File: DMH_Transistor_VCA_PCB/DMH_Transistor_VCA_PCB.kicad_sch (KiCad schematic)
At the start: 0 parts

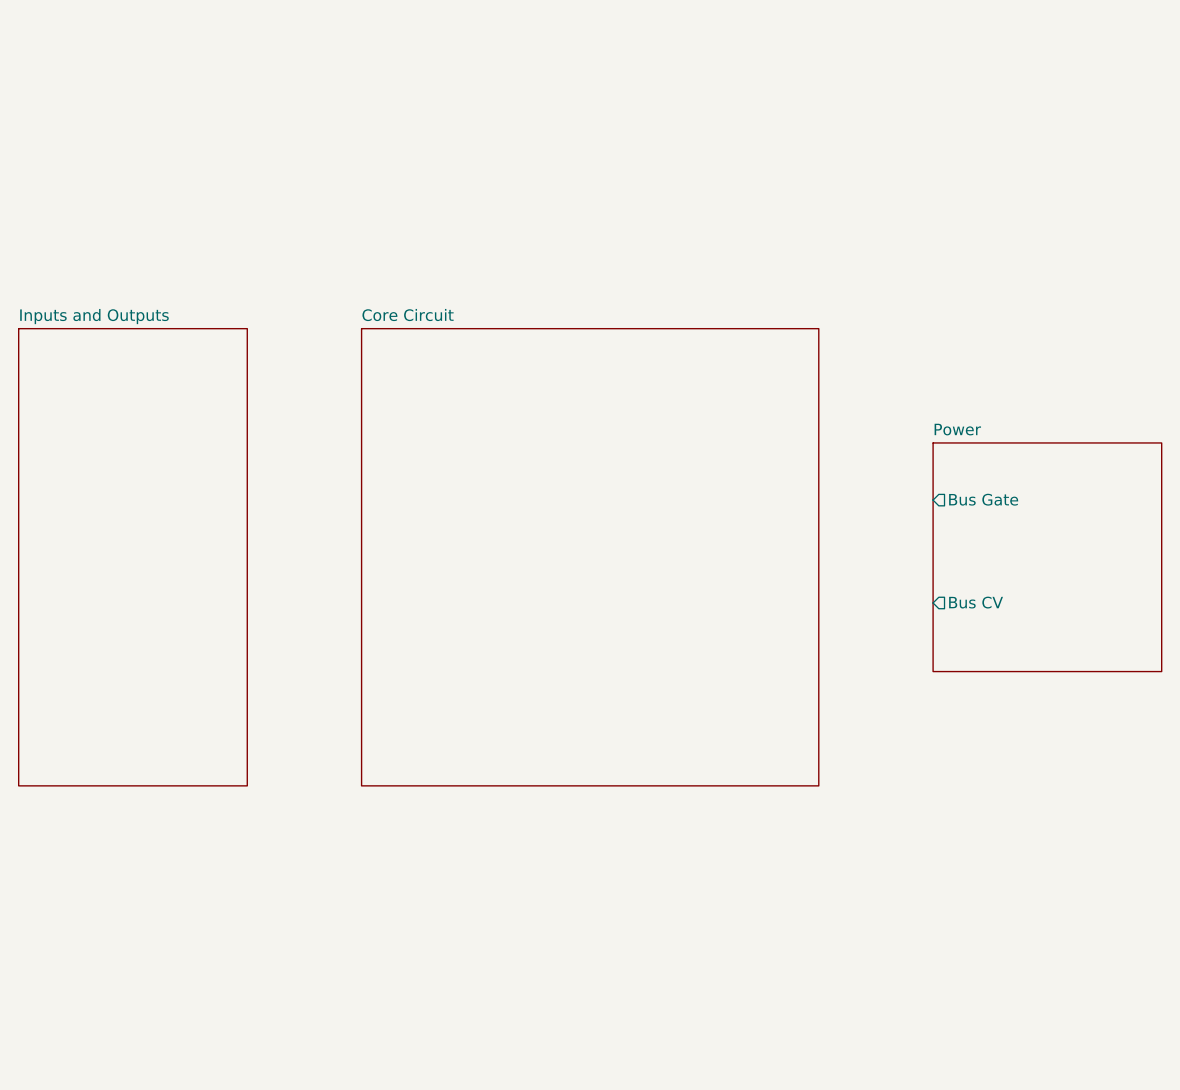
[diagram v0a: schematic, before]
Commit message: Finished core circuit schematic
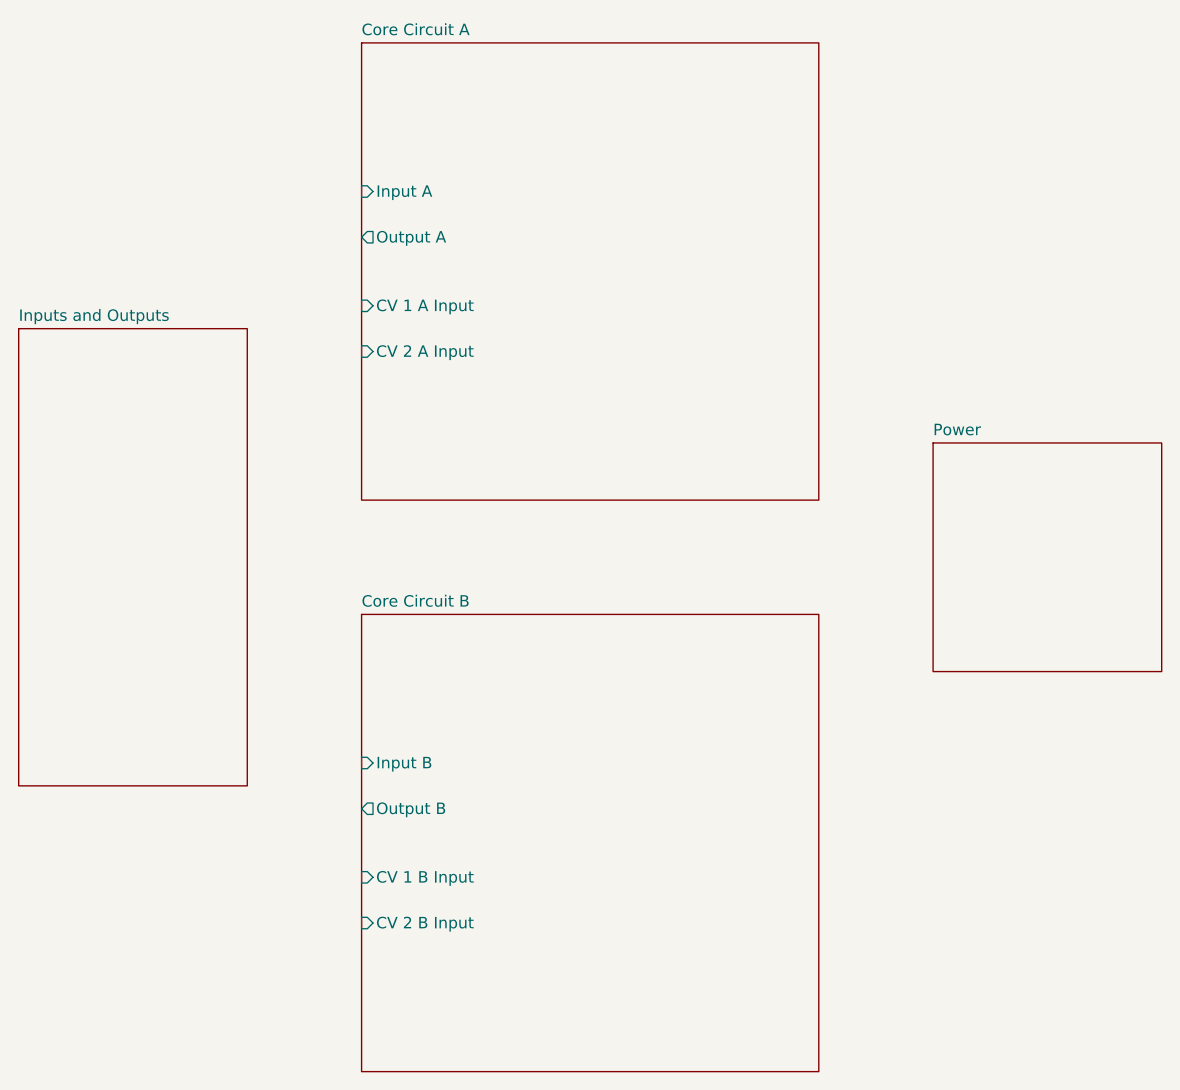
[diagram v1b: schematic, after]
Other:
- sheet Core Circuit renamed Core Circuit A
- added sheet Core Circuit B (Core_Circuit_B.kicad_sch)
- sheet Core Circuit A: file Core_Circuit.kicad_sch -> Core_Circuit_A.kicad_sch
- sheet Core Circuit A ports: added CV 1 A Input, CV 2 A Input, Input A, Output A; removed none
- sheet Power ports: added none; removed Bus CV, Bus Gate
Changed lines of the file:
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@@
-			)
-		)
-		(pin "Bus Gate" output
-			(at 127 95.25 180)
-			(effects
-				(font
-					(size 1.27 1.27)
-				)
-				(justify left)
-			)
-		)
-		(pin "Bus CV" output
-			(at 127 106.68 180)
-			(effects
-				(font
-					(size 1.27 1.27)
-				)
-				(justify left)
 			)
 		)
 		(instances
-			(project "DMH-Kosmo-5cm-PCB"
+			(project "DMH_Transistor_VCA_PCB"
 				(path "/58f4306d-5387-4983-bb08-41a2313fd315"
 					(page "4")
@@
 	)
 	(sheet
-		(at 63.5 76.2)
+		(at 63.5 107.95)
 		(size 50.8 50.8)
 		(fields_autoplaced yes)
@@
 			(color 0 0 0 0.0000)
 		)
-		(property "Sheetname" "Core Circuit"
-			(at 63.5 75.4884 0)
+		(property "Sheetname" "Core Circuit B"
+			(at 63.5 107.2384 0)
 			(effects
 				(font
@@
 			)
 		)
-		(property "Sheetfile" "Core_Circuit.kicad_sch"
-			(at 63.5 127.5846 0)
+		(property "Sheetfile" "Core_Circuit_B.kicad_sch"
+			(at 63.5 159.3346 0)
 			(effects
 				(font
@@
 			)
 		)
+		(pin "CV 1 B Input" input
+			(at 63.5 137.16 180)
+			(effects
+				(font
+					(size 1.27 1.27)
+				)
+				(justify left)
+			)
+		)
+		(pin "CV 2 B Input" input
+			(at 63.5 142.24 180)
+			(effects
+				(font
+					(size 1.27 1.27)
+				)
+				(justify left)
+			)
+		)
+		(pin "Input B" input
+			(at 63.5 124.46 180)
+			(effects
+				(font
+					(size 1.27 1.27)
+				)
+				(justify left)
+			)
+		)
+		(pin "Output B" output
+			(at 63.5 129.54 180)
+			(effects
+				(font
+					(size 1.27 1.27)
+				)
+				(justify left)
+			)
+		)
 		(instances
-			(project "DMH-Kosmo-5cm-PCB"
+			(project "DMH_Transistor_VCA_PCB"
+				(path "/58f4306d-5387-4983-bb08-41a2313fd315"
+					(page "5")
+				)
+			)
+		)
+	)
+	(sheet
+		(at 63.5 44.45)
+		(size 50.8 50.8)
+		(fields_autoplaced yes)
+		(stroke
+			(width 0.1524)
+			(type solid)
+		)
+		(fill
+			(color 0 0 0 0.0000)
+		)
+		(property "Sheetname" "Core Circuit A"
+			(at 63.5 43.7384 0)
+			(effects
+				(font
+					(size 1.27 1.27)
+				)
+				(justify left bottom)
+			)
+		)
+		(property "Sheetfile" "Core_Circuit_A.kicad_sch"
+			(at 63.5 95.8346 0)
+			(effects
+				(font
+					(size 1.27 1.27)
+				)
+				(justify left top)
+				(hide yes)
+			)
+		)
+		(pin "CV 1 A Input" input
+			(at 63.5 73.66 180)
+			(effects
+				(font
+					(size 1.27 1.27)
+				)
+				(justify left)
+			)
+		)
+		(pin "CV 2 A Input" input
+			(at 63.5 78.74 180)
+			(effects
+				(font
+					(size 1.27 1.27)
+				)
+				(justify left)
+			)
+		)
+		(pin "Input A" input
+			(at 63.5 60.96 180)
+			(effects
+				(font
+					(size 1.27 1.27)
+				)
+				(justify left)
+			)
+		)
+		(pin "Output A" output
+			(at 63.5 66.04 180)
+			(effects
+				(font
+					(size 1.27 1.27)
+				)
+				(justify left)
+			)
+		)
+		(instances
+			(project "DMH_Transistor_VCA_PCB"
 				(path "/58f4306d-5387-4983-bb08-41a2313fd315"
 					(page "3")
@@
 		)
 		(instances
-			(project "DMH-Kosmo-5cm-PCB"
+			(project "DMH_Transistor_VCA_PCB"
 				(path "/58f4306d-5387-4983-bb08-41a2313fd315"
 					(page "2")

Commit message: Finished schematic
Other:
- sheet Core Circuit A ports: added CV 1 A Pot, CV 2 A Pot; removed none
- sheet Core Circuit B ports: added CV 1 B Pot, CV 2 B Pot; removed none
- sheet Inputs and Outputs ports: added CV 1 A Jack, CV 1 A Pot, CV 1 B Jack, CV 1 B Pot, CV 2 A Jack, CV 2 A Pot, CV 2 B Jack, CV 2 B Pot, Input A Jack, Input B Jack, Output A Jack, Output B Jack; removed none

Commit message: Finished main PCB
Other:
- sheet Core Circuit A ports: added Offset A Pot; removed none
- sheet Core Circuit B ports: added Offset B Pot; removed none
- sheet Inputs and Outputs ports: added Offset A Pot, Offset B Pot; removed none
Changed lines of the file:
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@@
 	(wire
 		(pts
-			(xy 50.8 137.16) (xy 63.5 137.16)
-		)
-		(stroke
-			(width 0)
-			(type default)
-		)
-	)
-	(wire
-		(pts
-			(xy 50.8 132.08) (xy 63.5 132.08)
-		)
-		(stroke
-			(width 0)
-			(type default)
-		)
-	)
-	(wire
-		(pts
-			(xy 50.8 66.04) (xy 63.5 66.04)
-		)
-		(stroke
-			(width 0)
-			(type default)
-		)
-	)
-	(wire
-		(pts
-			(xy 50.8 142.24) (xy 63.5 142.24)
+			(xy 50.8 139.7) (xy 63.5 139.7)
+		)
+		(stroke
+			(width 0)
+			(type default)
+		)
+	)
+	(wire
+		(pts
+			(xy 50.8 134.62) (xy 63.5 134.62)
+		)
+		(stroke
+			(width 0)
+			(type default)
+		)
+	)
+	(wire
+		(pts
+			(xy 50.8 63.5) (xy 63.5 63.5)
+		)
+		(stroke
+			(width 0)
+			(type default)
+		)
+	)
+	(wire
+		(pts
+			(xy 50.8 144.78) (xy 63.5 144.78)
+		)
+		(stroke
+			(width 0)
+			(type default)
+		)
+	)
+	(wire
+		(pts
+			(xy 50.8 124.46) (xy 63.5 124.46)
+		)
+		(stroke
+			(width 0)
+			(type default)
+		)
+	)
+	(wire
+		(pts
+			(xy 50.8 68.58) (xy 63.5 68.58)
 		)
 		(stroke
@@
 	(wire
 		(pts
-			(xy 50.8 127) (xy 63.5 127)
+			(xy 50.8 129.54) (xy 63.5 129.54)
 		)
 		(stroke
@@
 	(wire
 		(pts
-			(xy 50.8 60.96) (xy 63.5 60.96)
+			(xy 50.8 58.42) (xy 63.5 58.42)
 		)
 		(stroke
@@
 		)
 		(pin "CV 1 B Input" input
-			(at 63.5 127 180)
+			(at 63.5 129.54 180)
 			(effects
 				(font
@@
 		)
 		(pin "CV 2 B Input" input
-			(at 63.5 137.16 180)
+			(at 63.5 139.7 180)
 			(effects
 				(font
@@
 		)
 		(pin "CV 1 B Pot" input
-			(at 63.5 132.08 180)
+			(at 63.5 134.62 180)
 			(effects
 				(font
@@
 		)
 		(pin "CV 2 B Pot" input
-			(at 63.5 142.24 180)
+			(at 63.5 144.78 180)
+			(effects
+				(font
+					(size 1.27 1.27)
+				)
+				(justify left)
+			)
+		)
+		(pin "Offset B Pot" input
+			(at 63.5 124.46 180)
 			(effects
 				(font
@@
 		)
 		(pin "Input A" input
-			(at 63.5 60.96 180)
+			(at 63.5 58.42 180)
 			(effects
 				(font
@@
 		)
 		(pin "Output A" output
-			(at 63.5 66.04 180)
+			(at 63.5 63.5 180)
 			(effects
 				(font
@@
 		(pin "CV 2 A Pot" input
 			(at 63.5 88.9 180)
+			(effects
+				(font
+					(size 1.27 1.27)
+				)
+				(justify left)
+			)
+		)
+		(pin "Offset A Pot" input
+			(at 63.5 68.58 180)
 			(effects
 				(font
@@
 		)
 		(pin "Output A Jack" input
-			(at 50.8 66.04 0)
+			(at 50.8 63.5 0)
 			(effects
 				(font
@@
 		)
 		(pin "Input A Jack" output
-			(at 50.8 60.96 0)
+			(at 50.8 58.42 0)
 			(effects
 				(font
@@
 		)
 		(pin "CV 1 B Jack" output
-			(at 50.8 127 0)
+			(at 50.8 129.54 0)
 			(effects
 				(font
@@
 		)
 		(pin "CV 2 B Jack" output
-			(at 50.8 137.16 0)
+			(at 50.8 139.7 0)
 			(effects
 				(font
@@
 		)
 		(pin "CV 1 B Pot" output
-			(at 50.8 132.08 0)
+			(at 50.8 134.62 0)
 			(effects
 				(font
@@
 		)
 		(pin "CV 2 B Pot" output
-			(at 50.8 142.24 0)
-			(effects
-				(font
+			(at 50.8 144.78 0)
+			(effects
+				(font
+					(size 1.27 1.27)
+				)
+				(justify right)
+			)
+		)
+		(pin "Offset B Pot" output
+			(at 50.8 124.46 0)
+			(effects
+				(font
+					(size 1.27 1.27)
+				)
+				(justify right)
+			)
+		)
+		(pin "Offset A Pot" output
+			(at 50.8 68.58 0)
+			(effects
+				(font
